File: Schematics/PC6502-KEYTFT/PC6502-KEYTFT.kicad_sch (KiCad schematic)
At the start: 47 parts, among them J1 BUS, J2 Conn_02x20_Odd_Even, J5 Conn_02x05_Odd_Even, J6 MTJ-88ARX1-FSM-LG, Q7 2N3904, Q8 2N3904, U1 W65C51NxP, U2 ATF1502AS, U21 AMS1117-3.3, U8 TXB0108PW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

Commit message: Update KeyTFT CPLD
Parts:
- removed U8, U9: TXB0108PW, Package_SO:TSSOP-20_4.4x6.5mm_P0.65mm, symbol Logic_LevelTranslator:TXB0108PW
- added U8, U9: TXS0108EPW, Package_SO:TSSOP-20_4.4x6.5mm_P0.65mm, symbol Logic_LevelTranslator:TXS0108EPW
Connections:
- net +3.3V: now also U8.10 (OE), U8.2 (VCCA), U9.10 (OE), U9.2 (VCCA)
- net +5V: now also U8.19 (VCCB), U9.19 (VCCB)
- net 3V3_BL: now also U8.9 (A8)
- net 3V3_D0: now also U9.1 (A1)
- net 3V3_D1: now also U9.3 (A2)
- net 3V3_D2: now also U9.4 (A3)
- net 3V3_D3: now also U9.5 (A4)
- net 3V3_D4: now also U9.6 (A5)
- net 3V3_D5: now also U9.7 (A6)
- net 3V3_D6: now also U9.8 (A7)
- net 3V3_D7: now also U9.9 (A8)
- net 3V3_EN: now also U8.1 (A1)
- net 3V3_RS: now also U8.8 (A7)
- net 3V3_RnW: now also U8.6 (A5)
- net 3V3_nCS: now also U8.3 (A2)
- net 3V3_nINT: now also U8.7 (A6)
- net 3V3_nWAIT: now also U8.4 (A3)
- net A0: now also U8.13 (B7)
- net BL: now also U8.12 (B8)
- net D0: now also U9.20 (B1)
- net D1: now also U9.18 (B2)
- net D2: now also U9.17 (B3)
- net D3: now also U9.16 (B4)
- net D4: now also U9.15 (B5)
- net D5: now also U9.14 (B6)
- net D6: now also U9.13 (B7)
- net D7: now also U9.12 (B8)
- net DISP_EN: now also U8.20 (B1)
- net DISP_nCS: now also U8.18 (B2)
- net DISP_nINT: now also U8.14 (B6)
- net DISP_nRES: now also U8.16 (B4)
- net DISP_nWAIT: now also U8.17 (B3)
- net GND: now also U8.11 (GND), U9.11 (GND)
- net RnW: now also U8.15 (B5)
- net at R67.1: now also U8.5 (A4)
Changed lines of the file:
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@@
 	)
 	(symbol
+		(lib_id "Logic_LevelTranslator:TXS0108EPW")
+		(at 171.45 57.15 0)
+		(unit 1)
+		(exclude_from_sim no)
+		(in_bom yes)
+		(on_board yes)
+		(dnp no)
+		(fields_autoplaced yes)
+		(property "Reference" "U8"
+			(at 173.5933 74.93 0)
+			(effects
+				(font
+					(size 1.27 1.27)
+				)
+				(justify left)
+			)
+		)
+		(property "Value" "TXS0108EPW"
+			(at 173.5933 77.47 0)
+			(effects
+				(font
+					(size 1.27 1.27)
+				)
+				(justify left)
+			)
+		)
+		(property "Footprint" "Package_SO:TSSOP-20_4.4x6.5mm_P0.65mm"
+			(at 171.45 76.2 0)
+			(effects
+				(font
+					(size 1.27 1.27)
+				)
+				(hide yes)
+			)
+		)
+		(property "Datasheet" "www.ti.com/lit/ds/symlink/txs0108e.pdf"
+			(at 171.45 59.69 0)
+			(effects
+				(font
+					(size 1.27 1.27)
+				)
+				(hide yes)
+			)
+		)
+		(property "Description" "Bidirectional  level-shifting voltage translator, TSSOP-20"
+			(at 171.45 57.15 0)
+			(effects
+				(font
+					(size 1.27 1.27)
+				)
+				(hide yes)
+			)
+		)
+		(pin "15"
+		)
+		(pin "20"
+		)
+		(pin "2"
+		)
+		(pin "4"
+		)
+		(pin "16"
+		)
+		(pin "11"
+		)
+		(pin "13"
+		)
+		(pin "12"
+		)
+		(pin "9"
+		)
+		(pin "19"
+		)
+		(pin "18"
+		)
+		(pin "5"
+		)
+		(pin "3"
+		)
+		(pin "1"
+		)
+		(pin "10"
+		)
+		(pin "7"
+		)
+		(pin "14"
+		)
+		(pin "8"
+		)
+		(pin "17"
+		)
+		(pin "6"
+		)
+		(instances
+			(project "PC6502-KEYTFT"
+				(path "/431ed1ef-9b76-40e5-9f99-258de85faf41"
+					(reference "U8")
+					(unit 1)
+				)
+			)
+		)
+	)
+	(symbol
 		(lib_id "Connector_Generic:Conn_02x20_Odd_Even")
 		(at 92.71 67.31 0)
@@
 	)
 	(symbol
+		(lib_id "Logic_LevelTranslator:TXS0108EPW")
+		(at 173.99 116.84 0)
+		(unit 1)
+		(exclude_from_sim no)
+		(in_bom yes)
+		(on_board yes)
+		(dnp no)
+		(fields_autoplaced yes)
+		(property "Reference" "U9"
+			(at 176.1333 134.62 0)
+			(effects
+				(font
+					(size 1.27 1.27)
+				)
+				(justify left)
+			)
+		)
+		(property "Value" "TXS0108EPW"
+			(at 176.1333 137.16 0)
+			(effects
+				(font
+					(size 1.27 1.27)
+				)
+				(justify left)
+			)
+		)
+		(property "Footprint" "Package_SO:TSSOP-20_4.4x6.5mm_P0.65mm"
+			(at 173.99 135.89 0)
+			(effects
+				(font
+					(size 1.27 1.27)
+				)
+				(hide yes)
+			)
+		)
+		(property "Datasheet" "www.ti.com/lit/ds/symlink/txs0108e.pdf"
+			(at 173.99 119.38 0)
+			(effects
+				(font
+					(size 1.27 1.27)
+				)
+				(hide yes)
+			)
+		)
+		(property "Description" "Bidirectional  level-shifting voltage translator, TSSOP-20"
+			(at 173.99 116.84 0)
+			(effects
+				(font
+					(size 1.27 1.27)
+				)
+				(hide yes)
+			)
+		)
+		(pin "15"
+		)
+		(pin "20"
+		)
+		(pin "2"
+		)
+		(pin "4"
+		)
+		(pin "16"
+		)
+		(pin "11"
+		)
+		(pin "13"
+		)
+		(pin "12"
+		)
+		(pin "9"
+		)
+		(pin "19"
+		)
+		(pin "18"
+		)
+		(pin "5"
+		)
+		(pin "3"
+		)
+		(pin "1"
+		)
+		(pin "10"
+		)
+		(pin "7"
+		)
+		(pin "14"
+		)
+		(pin "8"
+		)
+		(pin "17"
+		)
+		(pin "6"
+		)
+		(instances
+			(project ""
+				(path "/431ed1ef-9b76-40e5-9f99-258de85faf41"
+					(reference "U9")
+					(unit 1)
+				)
+			)
+		)
+	)
+	(symbol
 		(lib_id "power:+5V")
 		(at 288.29 87.63 0)
@@
 	)
 	(symbol
-		(lib_id "Logic_LevelTranslator:TXB0108PW")
-		(at 173.99 116.84 0)
-		(unit 1)
-		(exclude_from_sim no)
-		(in_bom yes)
-		(on_board yes)
-		(dnp no)
-		(property "Reference" "U9"
-			(at 176.1333 134.62 0)
-			(effects
-				(font
-					(size 1.27 1.27)
-				)
-				(justify left)
-			)
-		)
-		(property "Value" "TXB0108PW"
-			(at 176.1333 137.16 0)
-			(effects
-				(font
-					(size 1.27 1.27)
-				)
-				(justify left)
-			)
-		)
-		(property "Footprint" "Package_SO:TSSOP-20_4.4x6.5mm_P0.65mm"
-			(at 173.99 135.89 0)
-			(effects
-				(font
-					(size 1.27 1.27)
-				)
-				(hide yes)
-			)
-		)
-		(property "Datasheet" "http://www.ti.com/lit/ds/symlink/txb0108.pdf"
-			(at 173.99 119.38 0)
-			(effects
-				(font
-					(size 1.27 1.27)
-				)
-				(hide yes)
-			)
-		)
-		(property "Description" "8-Bit Bidirectional Voltage-Level Translator, Auto Direction Sensing and ±15-kV ESD Protection, 1.2 - 3.6V APort, 1.65 - 5.5V BPort, TSSOP-20"
-			(at 173.99 116.84 0)
-			(effects
-				(font
-					(size 1.27 1.27)
-				)
-				(hide yes)
-			)
-		)
-		(property "LCSC" "C53406"
-			(at 173.99 116.84 0)
-			(effects
-				(font
-					(size 1.27 1.27)
-				)
-			)
-		)
-		(property "Mouser Part Number" "595-TXB0108PWR"
-			(at 173.99 116.84 0)
-			(effects
-				(font
-					(size 1.27 1.27)
-				)
-				(hide yes)
-			)
-		)
-		(pin "4"
-		)
-		(pin "16"
-		)
-		(pin "3"
-		)
-		(pin "9"
-		)
-		(pin "6"
-		)
-		(pin "1"
-		)
-		(pin "10"
-		)
-		(pin "5"
-		)
-		(pin "19"
-		)
-		(pin "8"
-		)
-		(pin "2"
-		)
-		(pin "20"
-		)
-		(pin "11"
-		)
-		(pin "7"
-		)
-		(pin "18"
-		)
-		(pin "17"
-		)
-		(pin "15"
-		)
-		(pin "14"
-		)
-		(pin "13"
-		)
-		(pin "12"
-		)
-		(instances
-			(project "PC6502-KEYTFT"
-				(path "/431ed1ef-9b76-40e5-9f99-258de85faf41"
-					(reference "U9")
-					(unit 1)
-				)
-			)
-		)
-	)
-	(symbol
 		(lib_id "power:+3.3V")
 		(at 168.91 35.56 0)
@@
 					(unit 1)
 				)
-			)
-		)
-	)
-	(symbol
-		(lib_id "Logic_LevelTranslator:TXB0108PW")
-		(at 171.45 57.15 0)
-		(unit 1)
-		(exclude_from_sim no)
-		(in_bom yes)
-		(on_board yes)
-		(dnp no)
-		(property "Reference" "U8"
-			(at 173.5933 74.93 0)
-			(effects
-				(font
-					(size 1.27 1.27)
-				)
-				(justify left)
-			)
-		)
-		(property "Value" "TXB0108PW"
-			(at 173.5933 77.47 0)
-			(effects
-				(font
-					(size 1.27 1.27)
-				)
-				(justify left)
-			)
-		)
-		(property "Footprint" "Package_SO:TSSOP-20_4.4x6.5mm_P0.65mm"
-			(at 171.45 76.2 0)
-			(effects
-				(font
-					(size 1.27 1.27)
-				)
-				(hide yes)
-			)
-		)
-		(property "Datasheet" "http://www.ti.com/lit/ds/symlink/txb0108.pdf"
-			(at 171.45 59.69 0)
-			(effects
-				(font
-					(size 1.27 1.27)
-				)
-				(hide yes)
-			)
-		)
-		(property "Description" "8-Bit Bidirectional Voltage-Level Translator, Auto Direction Sensing and ±15-kV ESD Protection, 1.2 - 3.6V APort, 1.65 - 5.5V BPort, TSSOP-20"
-			(at 171.45 57.15 0)
-			(effects
-				(font
-					(size 1.27 1.27)
-				)
-				(hide yes)
-			)
-		)
-		(property "LCSC" "C53406"
-			(at 171.45 57.15 0)
-			(effects
-				(font
-					(size 1.27 1.27)
-				)
-			)
-		)
-		(property "Mouser Part Number" "595-TXB0108PWR"
-			(at 171.45 57.15 0)
-			(effects
-				(font
-					(size 1.27 1.27)
-				)
-				(hide yes)
-			)
-		)
-		(pin "4"
-		)
-		(pin "16"
-		)
-		(pin "3"
-		)
-		(pin "9"
-		)
-		(pin "6"
-		)
-		(pin "1"
-		)
-		(pin "10"
-		)
-		(pin "5"
-		)
-		(pin "19"
-		)
-		(pin "8"
-		)
-		(pin "2"
-		)
-		(pin "20"
-		)
-		(pin "11"
-		)
-		(pin "7"
-		)
-		(pin "18"
-		)
-		(pin "17"
-		)
-		(pin "15"
-		)
-		(pin "14"
-		)
-		(pin "13"
-		)
-		(pin "12"
-		)
-		(instances
-			(project "PC6502-KEYTFT"
-				(path "/431ed1ef-9b76-40e5-9f99-258de85faf41"
-					(reference "U8")
-					(unit 1)
-				)

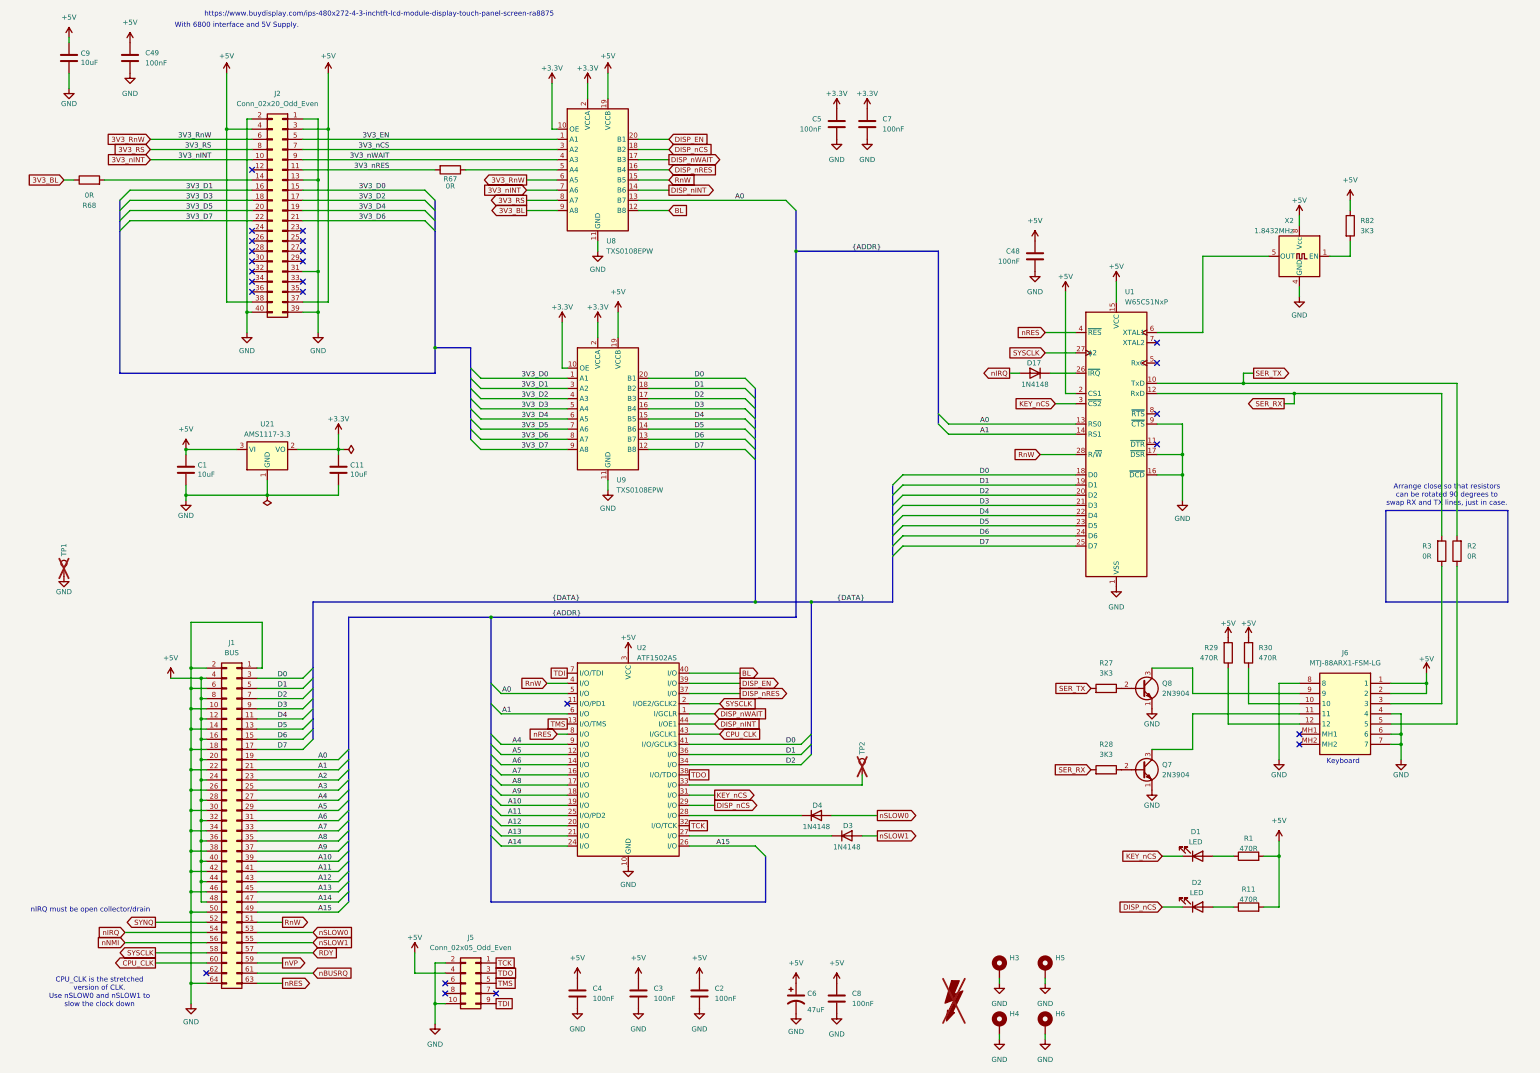
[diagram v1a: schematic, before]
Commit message: Updated KeyTFT Schematic to include mods
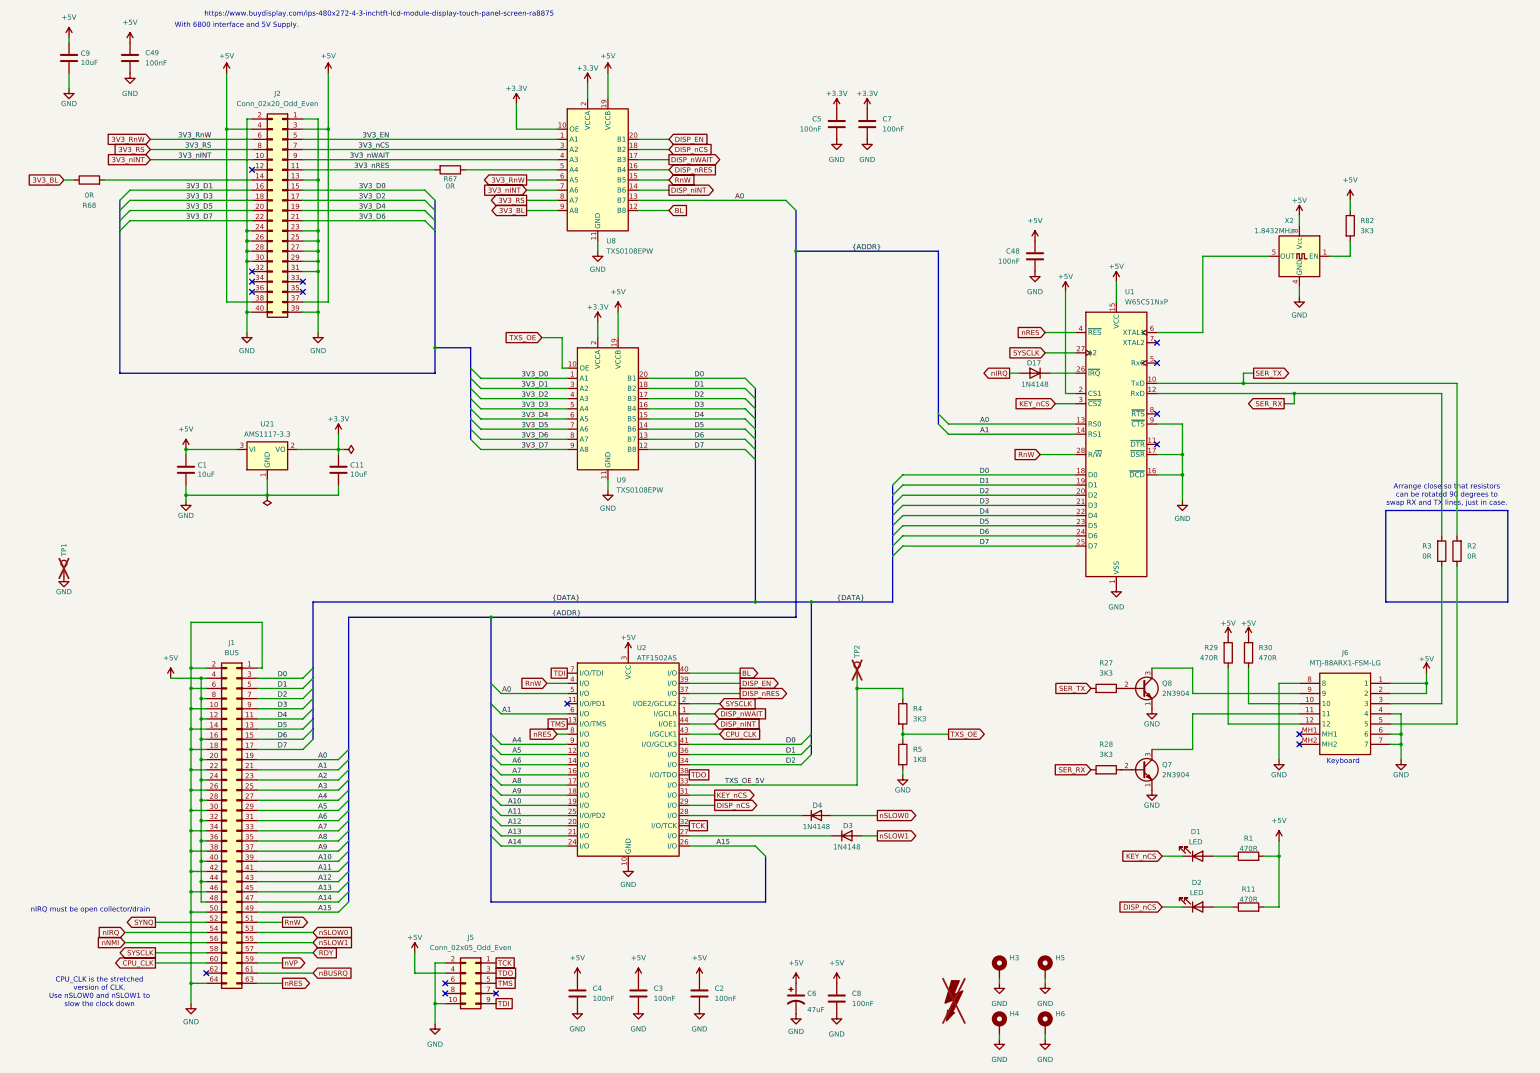
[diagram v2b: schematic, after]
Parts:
- added R4: 3K3, Resistor_SMD:R_0603_1608Metric, symbol Device:R
- added R5: 1K8, Resistor_SMD:R_0603_1608Metric, symbol Device:R
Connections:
- net +3.3V: no longer U9.10 (OE)
- net GND: now also J2.23 (Pin_23), J2.24 (Pin_24), J2.25 (Pin_25), J2.26 (Pin_26), J2.27 (Pin_27), J2.28 (Pin_28), J2.29 (Pin_29), J2.30 (Pin_30), R5.2
- net TXS_OE_5V: now reaches TP2.1, U2.33 (I/O)
- net TXS_OE_5V: now also R4.1
- new net TXS_OE: R4.2, R5.1, U9.10 (OE)
- no-connect marks 25 -> 17
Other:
- moved on the sheet: TP2

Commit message: Changes I forgot to commit
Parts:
- R4: value 3K3 -> 1K8
- R5: value 1K8 -> 3K3
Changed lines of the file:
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@@
 			)
 		)
-		(property "Value" "1K8"
+		(property "Value" "3K3"
 			(at 250.19 204.4699 0)
 			(effects
@@
 			)
 		)
-		(property "Value" "3K3"
+		(property "Value" "1K8"
 			(at 250.19 194.3099 0)
 			(effects
